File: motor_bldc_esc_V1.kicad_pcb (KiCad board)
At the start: 4 copper layers, 91.2 x 90.2 mm, 109 parts, among them J1 Conn_01x03_Socket, J2 Conn_01x03_Socket, J4 Conn_01x08_Socket, J5 Conn_01x02_Socket, J6 USB_C_Receptacle_USB2.0_16P, Q1 BSC060N10NS3G, Q2 BSC060N10NS3G, Q3 BSC060N10NS3G, Q4 BSC060N10NS3G, Q5 BSC060N10NS3G, Q6 BSC060N10NS3G, U1 DRV8353SRTAT, U2 ST STM32H563VIT6, U3 AM26LV32xD, U4 TLV75533PDBVR, U5 TI LM5164DDAR, U6 USBLC6-2SC6, U7 SN65HVD230DR, Y1 Crystal

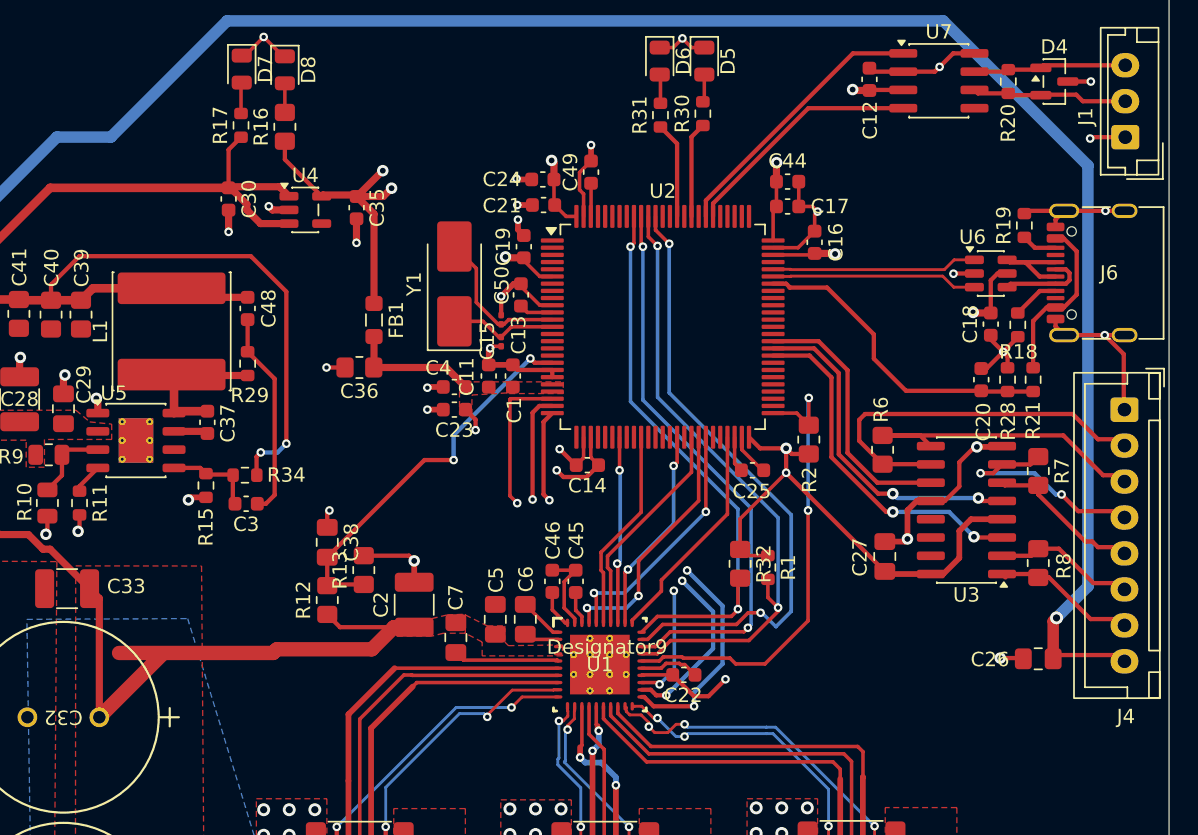
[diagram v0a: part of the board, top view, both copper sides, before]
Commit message: edit symbols because of DRC errors (DRV and LM5164)
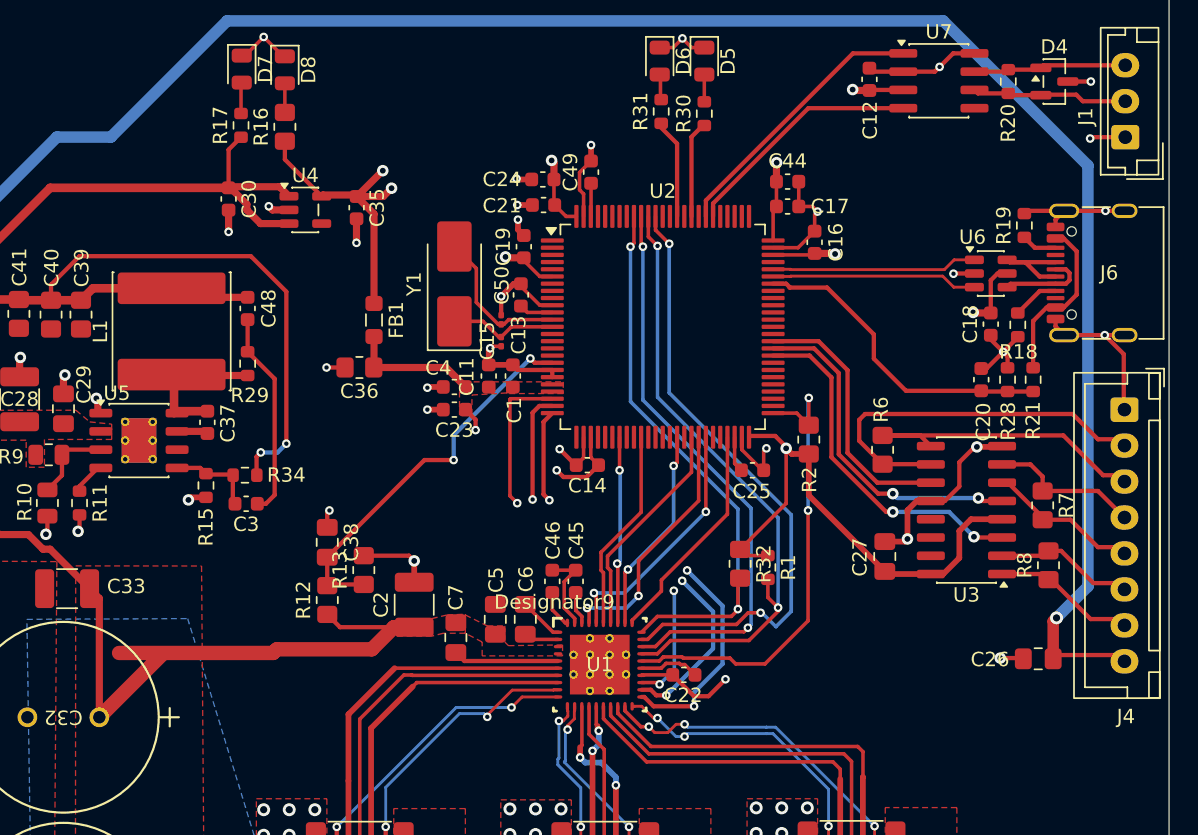
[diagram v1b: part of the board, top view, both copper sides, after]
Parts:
- D6: value LED_Status -> LED_Error
- R30, R31: value 220 -> 330
- U5: footprint Package_SO:HSOP-8-1EP_3.9x4.9mm_P1.27mm_EP2.41x3.1mm_ThermalVias -> Custom:LM5164DDAR
- moved R7 2.41 mm to (145.1, 117.7)
- moved R8 0.73 mm to (145.5, 121.8)
- moved R31 0.26 mm to (118.6, 90.3)
- moved U5 0.21 mm to (82.3, 113.1)
- moved R30 0.10 mm to (121.6, 90.4)
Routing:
- net Net-(J4-Pin_4): track 15.5 -> 10.6 mm, vias 2 -> 0
- net GND: track 188.9 -> 190.5 mm, vias 85 -> 86
- net +3.3V: track 91.8 -> 92.6 mm, vias 11 -> 10
- net Net-(J4-Pin_6): track 10.2 -> 9.70 mm

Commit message: update pcb (no errors with XRC)
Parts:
- added C34: 100n, Capacitor_SMD:C_0603_1608Metric, F.Cu at (103.5, 93.6)
- added J3: Conn_ARM_JTAG_SWD_10, Connector_PinHeader_1.27mm:PinHeader_2x05_P1.27mm_Vertical, F.Cu at (102.7, 86.2)
- added R33: 10k, Resistor_SMD:R_0805_2012Metric_Pad1.20x1.40mm_HandSolder, F.Cu at (115.8, 93.4)
- added R35: 10k, Resistor_SMD:R_0805_2012Metric_Pad1.20x1.40mm_HandSolder, F.Cu at (107.5, 92.3)
- C13, C15: footprint Capacitor_SMD:C_0201_0603Metric -> Capacitor_SMD:C_0603_1608Metric
- C31, C32: footprint Custom:100ZLJ330M12.5X35 -> MyLib:100ZLJ330M12.5X35
- U1: footprint Custom:DRV8353SRTAT -> MyLib:DRV8353SRTAT
- U5: footprint Custom:LM5164DDAR -> MyLib:LM5164DDAR
- moved C13 2.42 mm to (106.8, 102.4)
- moved Y1 1.68 mm to (103.6, 103.8)
- moved C15 0.81 mm to (106.8, 105.8)
- moved C23 0.51 mm to (104.3, 111.5)
- moved C1 0.46 mm to (108.3, 109.1)
- moved C11 0.46 mm to (106.7, 109.1)
- moved C4 0.46 mm to (104.3, 109.9)
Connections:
- U2 pad 14: unconnected-(U2-NRST-Pad14) -> /mcu/Reset
- U2 pad 78: unconnected-(U2-PC10-Pad78) -> /PowerStage/SerialCLK
- U2 pad 79: unconnected-(U2-PC11-Pad79) -> /PowerStage/SerialDataOutput
- U2 pad 80: unconnected-(U2-PC12-Pad80) -> /PowerStage/SerialDataInput
- U2 pad 89: /PowerStage/SerialCLK -> /mcu/SWO
- U2 pad 90: /PowerStage/SerialDataOutput -> unconnected-(U2-PB4(NJTRST)-Pad90)
- U2 pad 91: /PowerStage/SerialDataInput -> unconnected-(U2-PB5-Pad91)
- U2 pad 94: unconnected-(U2-BOOT0-Pad94) -> Net-(U2-BOOT0)
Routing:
- net /mcu/SWCLK: track 0.00 -> 31.6 mm, vias 0 -> 2
- net /mcu/SWDIO: track 0.00 -> 26.6 mm, vias 0 -> 2
- net /mcu/Reset: track 0.00 -> 24.4 mm, vias 0 -> 2
- net GND: track 190.5 -> 212.1 mm
- net /mcu/SWO: track 0.00 -> 20.4 mm
- net +3.3V: track 92.6 -> 106.0 mm, vias 10 -> 11
- net Net-(U2-BOOT0): track 0.00 -> 3.15 mm
- net /PowerStage/SerialDataOutput: track 44.2 -> 41.9 mm
- net /PowerStage/SerialCLK: track 43.4 -> 41.2 mm
- net /PowerStage/SerialDataInput: track 39.8 -> 37.8 mm
- net /mcu/RCC_OSC_IN: track 10.6 -> 8.93 mm
- net /PowerStage/U_Current_Sense: track 32.0 -> 31.1 mm
- net /mcu/RCC_OSC_OUT: track 7.55 -> 8.10 mm

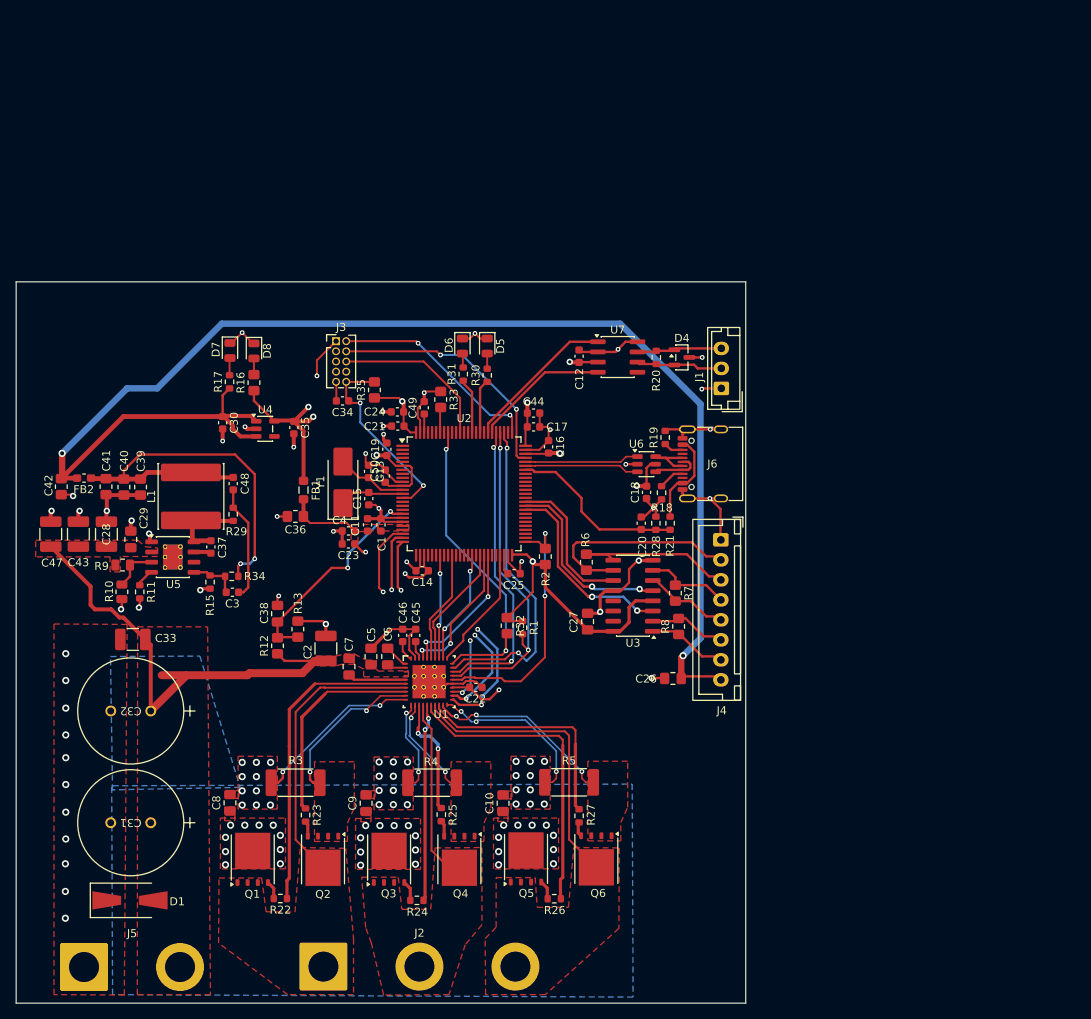
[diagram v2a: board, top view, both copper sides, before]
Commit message: finished design of PCB
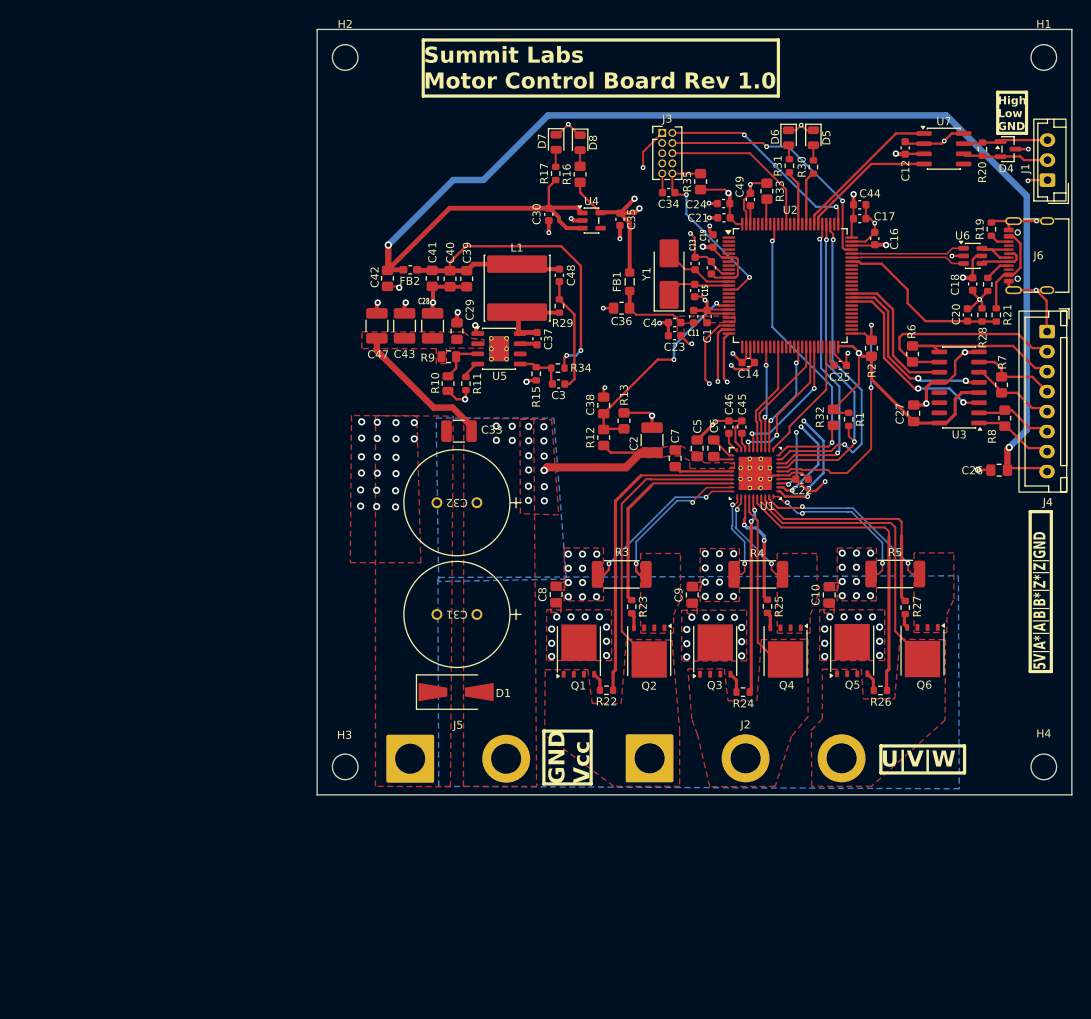
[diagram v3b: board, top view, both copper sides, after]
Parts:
- added H1: MountingHole, MountingHole:MountingHole_3.2mm_M3, F.Cu at (191.2, 50.7)
- added H2: MountingHole, MountingHole:MountingHole_3.2mm_M3, F.Cu at (103.9, 50.7)
- added H3: MountingHole, MountingHole:MountingHole_3.2mm_M3, F.Cu at (103.9, 139.4)
- added H4: MountingHole, MountingHole:MountingHole_3.2mm_M3, F.Cu at (191.2, 139.4)
- moved C13 48.4 mm to (147.6, 76.5), turned to 90 degrees
- moved C9 48.4 mm to (147.2, 117.9)
- moved Q6 48.4 mm to (176.0, 124.8)
- moved U7 48.4 mm to (178.7, 62.1)
- moved C10 48.4 mm to (164.4, 117.9)
- moved C18 48.4 mm to (182.3, 79.0)
- moved C2 48.4 mm to (142.2, 98.5)
- moved C23 48.4 mm to (145.0, 85.5)
- moved C30 48.4 mm to (129.3, 70.3)
- moved C31 48.4 mm to (120.3, 120.3)
- moved C32 48.4 mm to (120.3, 106.3)
- moved C4 48.4 mm to (145.0, 83.8)
- moved C7 48.4 mm to (145.1, 100.8)
- moved C8 48.4 mm to (130.2, 117.8)
- moved D1 48.4 mm to (117.7, 130.0)
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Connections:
- C13 pad 1: GND -> /mcu/RCC_OSC_IN
- C13 pad 2: /mcu/RCC_OSC_IN -> GND
- C15 pad 1: GND -> /mcu/RCC_OSC_OUT
- C15 pad 2: /mcu/RCC_OSC_OUT -> GND
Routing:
- net VCC: track 61.1 -> 38.7 mm, vias 30 -> 46
- net GND: track 212.1 -> 214.6 mm, vias 86 -> 94
- net /PowerStage/W_Shunt_P: track 24.0 -> 23.6 mm, vias 3 -> 2
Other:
- board size 91.2 x 90.2 mm -> 94.3 x 95.7 mm
- board text added: "5V|A*|A|B|B*|Z*|Z|GND"
- board text added: "GND"
- board text added: "High Low GND"
- board text added: "Summit Labs Motor Control Board Rev 1.0"
- board text added: "U|V|W"
- board text added: "Vcc"

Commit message: changes MCU because of stock
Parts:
- removed U2: ST STM32H563VIT6, Package_QFP:LQFP-100_14x14mm_P0.5mm
- added U8: STM32H523VET6, Package_QFP:LQFP-100_14x14mm_P0.5mm, F.Cu at (159.5, 79.2)
- D7: value LED_Status -> LED_5V
- D8: value LED_Status -> LED_3V3
- moved J3 22.3 mm to (165.8, 60.4), turned to -90 degrees
- moved C34 15.4 mm to (158.3, 61.2), turned to 90 degrees
- moved D5 14.3 mm to (148.4, 58.1), turned to 0 degrees
- moved R30 12.1 mm to (152.0, 58.1), turned to 180 degrees
- moved D6 10.9 mm to (148.4, 61.2), turned to 0 degrees
- moved R31 8.16 mm to (151.9, 61.1), turned to 180 degrees
- moved J6 0.66 mm to (191.2, 75.4)
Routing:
- net /mcu/SWCLK: track 31.6 -> 10.3 mm
- net /mcu/SWDIO: track 26.6 -> 14.2 mm
- net Net-(U8-PD3): track 6.64 -> 17.6 mm, vias 0 -> 2
- net /mcu/Reset: track 24.4 -> 34.5 mm
- net /mcu/SWO: track 20.4 -> 11.7 mm
- net Net-(U8-PD5): track 6.70 -> 14.9 mm, vias 0 -> 2
- net +3.3V: track 106.0 -> 104.0 mm
- net +5V: track 173.3 -> 171.5 mm
- net Net-(J6-VBUS-PadA4): track 11.9 -> 12.6 mm
- net /communication/D-: track 6.12 -> 6.78 mm
- net Net-(J6-CC1): track 3.26 -> 3.93 mm
- net Net-(J6-CC2): track 2.47 -> 3.12 mm
